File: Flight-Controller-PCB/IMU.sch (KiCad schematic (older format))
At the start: 13 parts, among them Q1 BSS138, Q2 BSS138, U2 ICM-20689

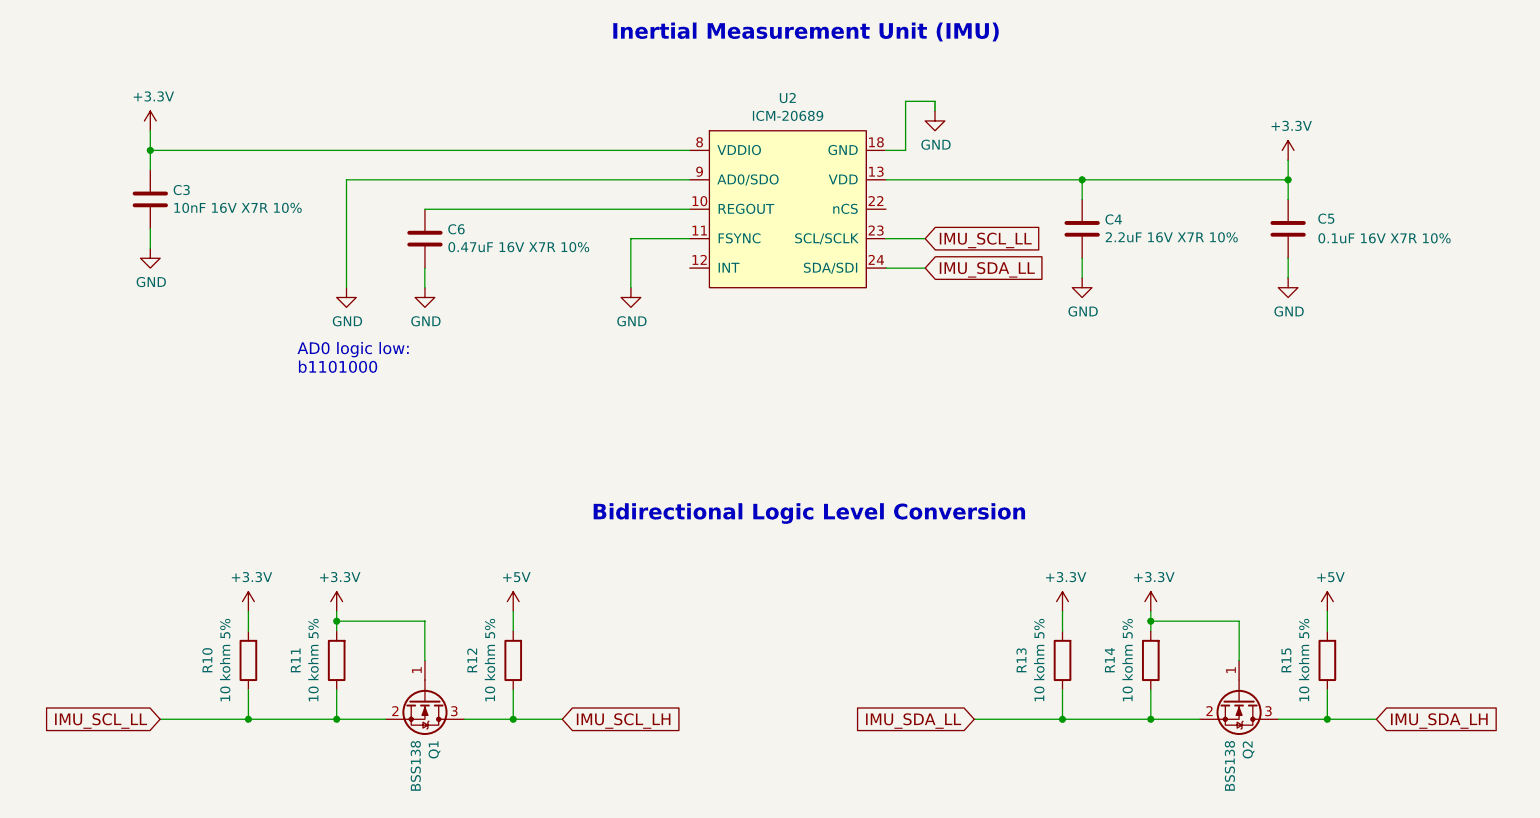
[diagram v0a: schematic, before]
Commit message: Deleted majority of unused components. Started schematic for new MCU
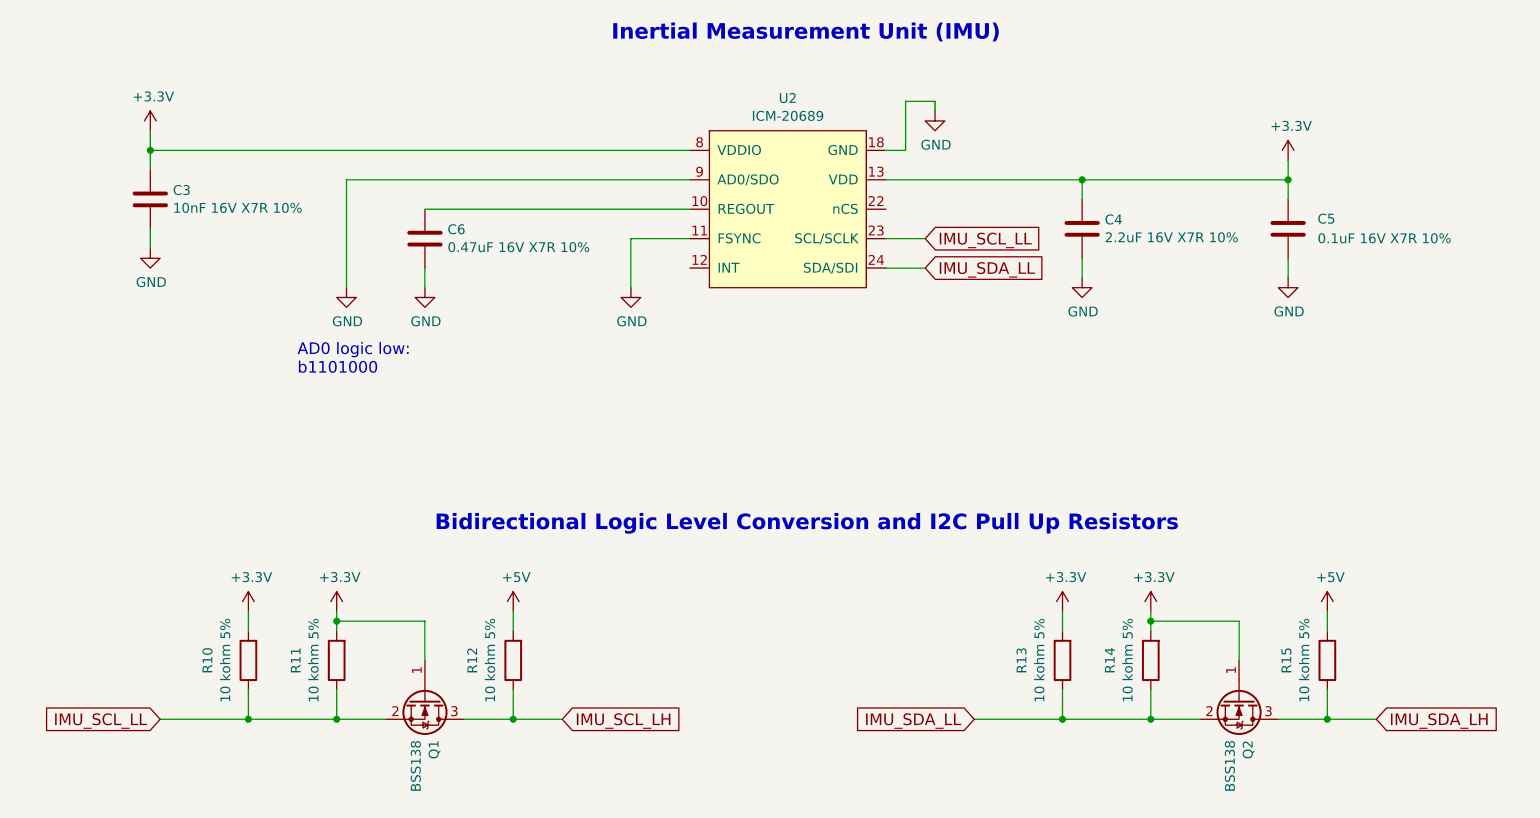
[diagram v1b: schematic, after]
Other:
- note added: "Bidirectional Logic Level Conversion and I2C Pull Up Resistors"
- note removed: "Bidirectional Logic Level Conversion"
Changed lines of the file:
@@
 EESchema Schematic File Version 4
-LIBS:Main-Board-cache
 EELAYER 30 0
 EELAYER END
@@
 Text Notes 4650 1800 0    79   ~ 16
 Inertial Measurement Unit (IMU)
-Text Notes 4550 4250 0    79   ~ 16
-Bidirectional Logic Level Conversion
+Text Notes 3750 4300 0    79   ~ 16
+Bidirectional Logic Level Conversion and I2C Pull Up Resistors
 $EndSCHEMATC

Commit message: Power Management and Selection roughed out
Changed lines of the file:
@@
 AR Path="/5FD99B6C/5FD9D006" Ref="Q1"  Part="1"
 AR Path="/5FD9E07D/5FD9D006" Ref="Q?"  Part="1"
-F 0 "Q1" H 3906 5196 50  0000 L CNN
-F 1 "BSS138" H 3906 5105 50  0000 L CNN
+F 0 "Q1" V 3951 5150 50  0000 C CNN
+F 1 "BSS138" V 4042 5150 50  0000 C CNN
 F 2 "Package_TO_SOT_SMD:SOT-23" H 3900 5075 50  0001 L CIN
 F 3 "" H 3700 5150 50  0001 L CNN
@@
 AR Path="/5FD99B6C/60033880" Ref="Q2"  Part="1"
 AR Path="/5FD9E07D/60033880" Ref="Q?"  Part="1"
-F 0 "Q2" H 8056 5196 50  0000 L CNN
-F 1 "BSS138" H 8056 5105 50  0000 L CNN
+F 0 "Q2" V 8101 5150 50  0000 C CNN
+F 1 "BSS138" V 8192 5150 50  0000 C CNN
 F 2 "Package_TO_SOT_SMD:SOT-23" H 8050 5075 50  0001 L CIN
 F 3 "" H 7850 5150 50  0001 L CNN

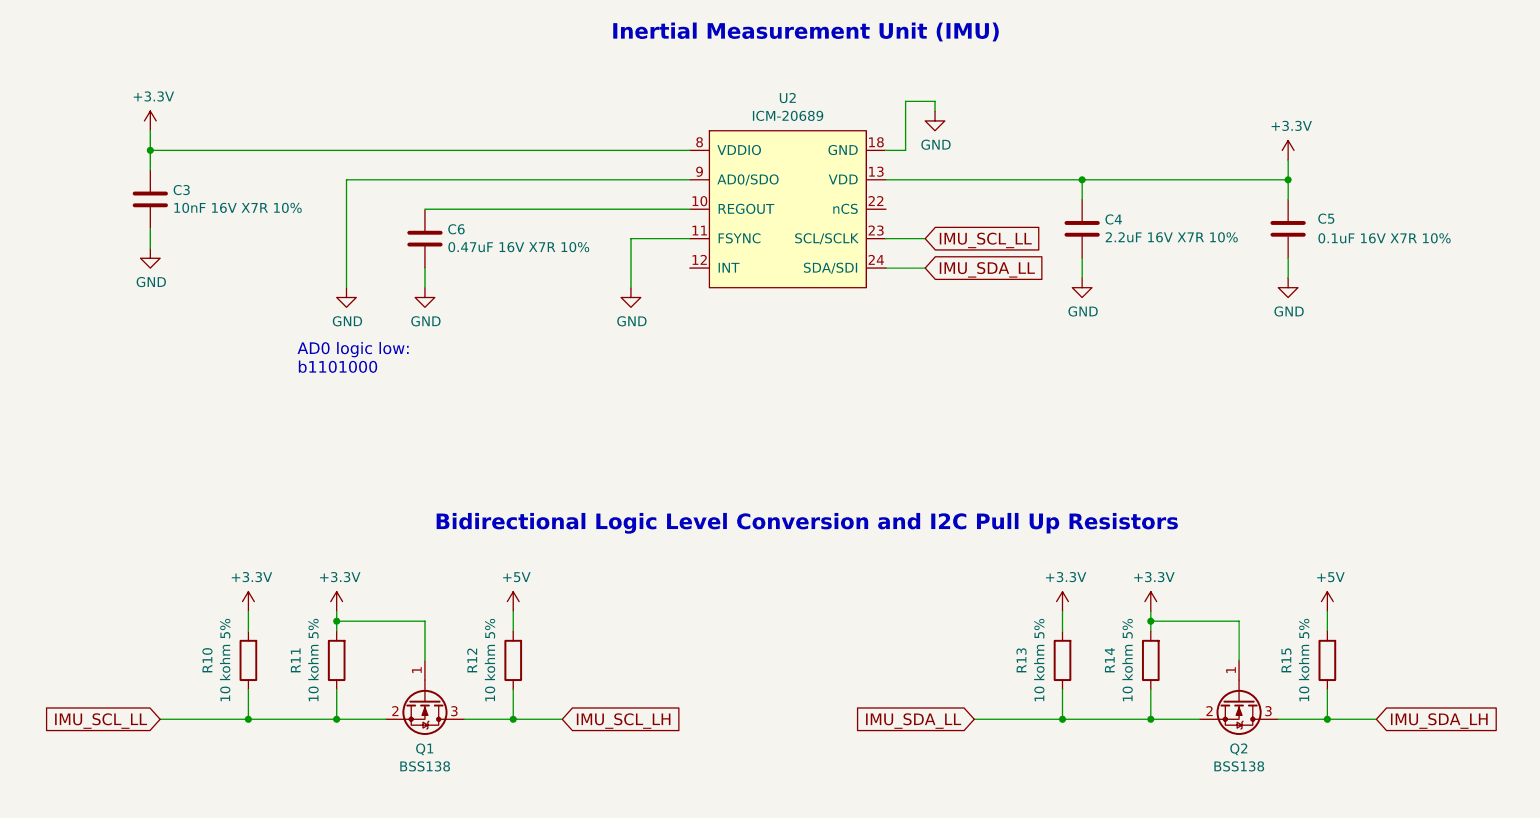
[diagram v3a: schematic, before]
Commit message: Updated pin mappings
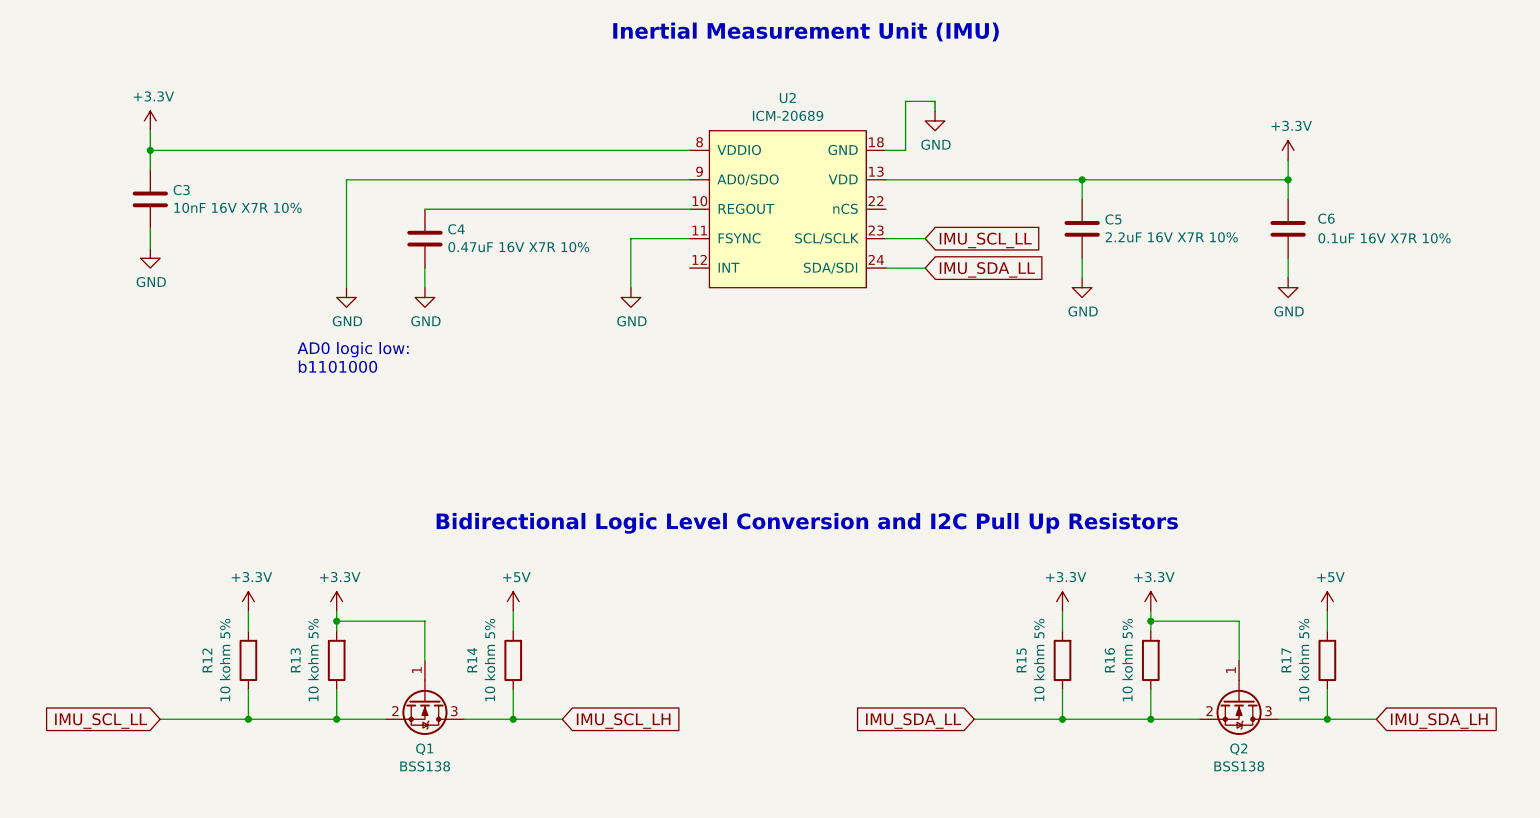
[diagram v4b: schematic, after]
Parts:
- renumbered C6 to C4, C4 to C5, C5 to C6, R10 to R12, R11 to R13, R12 to R14, R13 to R15, R14 to R16, R15 to R17
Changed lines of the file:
@@
 IMU_SCL_LL
 $Comp
-L power:+3.3V #PWR031
+L power:+3.3V #PWR030
 U 1 1 5FD9D00C
 P 2800 4700
-AR Path="/5FD99B6C/5FD9D00C" Ref="#PWR031"  Part="1"
+AR Path="/5FD99B6C/5FD9D00C" Ref="#PWR030"  Part="1"
 AR Path="/5FD9E07D/5FD9D00C" Ref="#PWR?"  Part="1"
-F 0 "#PWR031" H 2800 4550 50  0001 C CNN
+F 0 "#PWR030" H 2800 4550 50  0001 C CNN
 F 1 "+3.3V" H 2815 4873 50  0000 C CNN
 F 2 "" H 2800 4700 50  0001 C CNN
@@
 	5050 2800 4750 2800
 $Comp
-L power:GND #PWR030
+L power:GND #PWR035
 U 1 1 5FD9CFF8
 P 4750 3050
-AR Path="/5FD99B6C/5FD9CFF8" Ref="#PWR030"  Part="1"
+AR Path="/5FD99B6C/5FD9CFF8" Ref="#PWR035"  Part="1"
 AR Path="/5FD9E07D/5FD9CFF8" Ref="#PWR?"  Part="1"
-F 0 "#PWR030" H 4750 2800 50  0001 C CNN
+F 0 "#PWR035" H 4750 2800 50  0001 C CNN
 F 1 "GND" H 4755 2877 50  0000 C CNN
 F 2 "" H 4750 3050 50  0001 C CNN
@@
 	3300 2500 3300 3050
 $Comp
-L power:GND #PWR028
+L power:GND #PWR032
 U 1 1 5FD9CFEF
 P 3300 3050
-AR Path="/5FD99B6C/5FD9CFEF" Ref="#PWR028"  Part="1"
+AR Path="/5FD99B6C/5FD9CFEF" Ref="#PWR032"  Part="1"
 AR Path="/5FD9E07D/5FD9CFEF" Ref="#PWR?"  Part="1"
-F 0 "#PWR028" H 3300 2800 50  0001 C CNN
+F 0 "#PWR032" H 3300 2800 50  0001 C CNN
 F 1 "GND" H 3305 2877 50  0000 C CNN
 F 2 "" H 3300 3050 50  0001 C CNN
@@
 	3700 3050 3700 2950
 $Comp
-L power:GND #PWR029
+L power:GND #PWR033
 U 1 1 5FD9CFE8
 P 3700 3050
-AR Path="/5FD99B6C/5FD9CFE8" Ref="#PWR029"  Part="1"
+AR Path="/5FD99B6C/5FD9CFE8" Ref="#PWR033"  Part="1"
 AR Path="/5FD9E07D/5FD9CFE8" Ref="#PWR?"  Part="1"
-F 0 "#PWR029" H 3700 2800 50  0001 C CNN
+F 0 "#PWR033" H 3700 2800 50  0001 C CNN
 F 1 "GND" H 3705 2877 50  0000 C CNN
 F 2 "" H 3700 3050 50  0001 C CNN
@@
 	6050 2500 7050 2500
 $Comp
-L power:GND #PWR027
+L power:GND #PWR041
 U 1 1 5FD9CFD9
 P 8100 3000
-AR Path="/5FD99B6C/5FD9CFD9" Ref="#PWR027"  Part="1"
+AR Path="/5FD99B6C/5FD9CFD9" Ref="#PWR041"  Part="1"
 AR Path="/5FD9E07D/5FD9CFD9" Ref="#PWR?"  Part="1"
-F 0 "#PWR027" H 8100 2750 50  0001 C CNN
+F 0 "#PWR041" H 8100 2750 50  0001 C CNN
 F 1 "GND" H 8105 2827 50  0000 C CNN
 F 2 "" H 8100 3000 50  0001 C CNN
@@
 $EndComp
 $Comp
-L power:GND #PWR026
+L power:GND #PWR038
 U 1 1 5FD9CFD3
 P 7050 3000
-AR Path="/5FD99B6C/5FD9CFD3" Ref="#PWR026"  Part="1"
+AR Path="/5FD99B6C/5FD9CFD3" Ref="#PWR038"  Part="1"
 AR Path="/5FD9E07D/5FD9CFD3" Ref="#PWR?"  Part="1"
-F 0 "#PWR026" H 7050 2750 50  0001 C CNN
+F 0 "#PWR038" H 7050 2750 50  0001 C CNN
 F 1 "GND" H 7055 2827 50  0000 C CNN
 F 2 "" H 7050 3000 50  0001 C CNN
@@
 	6050 2350 6150 2350
 $Comp
-L power:+3.3V #PWR024
+L power:+3.3V #PWR040
 U 1 1 5FD9CFC9
 P 8100 2400
-AR Path="/5FD99B6C/5FD9CFC9" Ref="#PWR024"  Part="1"
+AR Path="/5FD99B6C/5FD9CFC9" Ref="#PWR040"  Part="1"
 AR Path="/5FD9E07D/5FD9CFC9" Ref="#PWR?"  Part="1"
-F 0 "#PWR024" H 8100 2250 50  0001 C CNN
+F 0 "#PWR040" H 8100 2250 50  0001 C CNN
 F 1 "+3.3V" H 8115 2573 50  0000 C CNN
 F 2 "" H 8100 2400 50  0001 C CNN
@@
 	2300 2250 2300 2350
 $Comp
-L power:GND #PWR025
+L power:GND #PWR029
 U 1 1 5FD9CFBF
 P 2300 2850
-AR Path="/5FD99B6C/5FD9CFBF" Ref="#PWR025"  Part="1"
+AR Path="/5FD99B6C/5FD9CFBF" Ref="#PWR029"  Part="1"
 AR Path="/5FD9E07D/5FD9CFBF" Ref="#PWR?"  Part="1"
-F 0 "#PWR025" H 2300 2600 50  0001 C CNN
+F 0 "#PWR029" H 2300 2600 50  0001 C CNN
 F 1 "GND" H 2305 2677 50  0000 C CNN
 F 2 "" H 2300 2850 50  0001 C CNN
@@
 $EndComp
 $Comp
-L power:+3.3V #PWR023
+L power:+3.3V #PWR028
 U 1 1 5FD9CFB9
 P 2300 2250
-AR Path="/5FD99B6C/5FD9CFB9" Ref="#PWR023"  Part="1"
+AR Path="/5FD99B6C/5FD9CFB9" Ref="#PWR028"  Part="1"
 AR Path="/5FD9E07D/5FD9CFB9" Ref="#PWR?"  Part="1"
-F 0 "#PWR023" H 2300 2100 50  0001 C CNN
+F 0 "#PWR028" H 2300 2100 50  0001 C CNN
 F 1 "+3.3V" H 2315 2423 50  0000 C CNN
 F 2 "" H 2300 2250 50  0001 C CNN
@@
 $EndComp
 $Comp
-L Device:R R10
+L Device:R R12
 U 1 1 5FD9CFB3
 P 2800 4950
-AR Path="/5FD99B6C/5FD9CFB3" Ref="R10"  Part="1"
+AR Path="/5FD99B6C/5FD9CFB3" Ref="R12"  Part="1"
 AR Path="/5FD9E07D/5FD9CFB3" Ref="R?"  Part="1"
-F 0 "R10" V 3007 4950 50  0000 C CNN
+F 0 "R12" V 3007 4950 50  0000 C CNN
 F 1 "10 kohm 5%" V 2916 4950 50  0000 C CNN
 F 2 "Resistor_SMD:R_0603_1608Metric_Pad1.05x0.95mm_HandSolder" V 2730 4950 50  0001 C CNN
@@
 $EndComp
 $Comp
-L power:GND #PWR022
+L power:GND #PWR036
 U 1 1 5FD9CFAD
 P 6300 2150
-AR Path="/5FD99B6C/5FD9CFAD" Ref="#PWR022"  Part="1"
+AR Path="/5FD99B6C/5FD9CFAD" Ref="#PWR036"  Part="1"
 AR Path="/5FD9E07D/5FD9CFAD" Ref="#PWR?"  Part="1"
-F 0 "#PWR022" H 6300 1900 50  0001 C CNN
+F 0 "#PWR036" H 6300 1900 50  0001 C CNN
 F 1 "GND" H 6305 1977 50  0000 C CNN
 F 2 "" H 6300 2150 50  0001 C CNN
@@
 $EndComp
 $Comp
-L Device:C C4
+L Device:C C5
 U 1 1 5FD9CFA1
 P 7050 2750
-AR Path="/5FD99B6C/5FD9CFA1" Ref="C4"  Part="1"
+AR Path="/5FD99B6C/5FD9CFA1" Ref="C5"  Part="1"
 AR Path="/5FD9E07D/5FD9CFA1" Ref="C?"  Part="1"
-F 0 "C4" H 7165 2796 50  0000 L CNN
+F 0 "C5" H 7165 2796 50  0000 L CNN
 F 1 "2.2uF 16V X7R 10%" H 7165 2705 50  0000 L CNN
 F 2 "Capacitor_SMD:C_0603_1608Metric_Pad1.05x0.95mm_HandSolder" H 7088 2600 50  0001 C CNN
@@
 $EndComp
 $Comp
-L Device:C C6
+L Device:C C4
 U 1 1 5FD9CF95
 P 3700 2800
-AR Path="/5FD99B6C/5FD9CF95" Ref="C6"  Part="1"
+AR Path="/5FD99B6C/5FD9CF95" Ref="C4"  Part="1"
 AR Path="/5FD9E07D/5FD9CF95" Ref="C?"  Part="1"
-F 0 "C6" H 3815 2846 50  0000 L CNN
+F 0 "C4" H 3815 2846 50  0000 L CNN
 F 1 "0.47uF 16V X7R 10%" H 3815 2755 50  0000 L CNN
 F 2 "Capacitor_SMD:C_0603_1608Metric_Pad1.05x0.95mm_HandSolder" H 3738 2650 50  0001 C CNN
@@
 $EndComp
 $Comp
-L Device:R R11
+L Device:R R13
 U 1 1 5FDA5523
 P 3250 4950
-AR Path="/5FD99B6C/5FDA5523" Ref="R11"  Part="1"
+AR Path="/5FD99B6C/5FDA5523" Ref="R13"  Part="1"
 AR Path="/5FD9E07D/5FDA5523" Ref="R?"  Part="1"
-F 0 "R11" V 3457 4950 50  0000 C CNN
+F 0 "R13" V 3457 4950 50  0000 C CNN
 F 1 "10 kohm 5%" V 3366 4950 50  0000 C CNN
 F 2 "Resistor_SMD:R_0603_1608Metric_Pad1.05x0.95mm_HandSolder" V 3180 4950 50  0001 C CNN
@@
 $EndComp
 $Comp
-L power:+3.3V #PWR032
+L power:+3.3V #PWR031
 U 1 1 5FDA626A
 P 3250 4700
-AR Path="/5FD99B6C/5FDA626A" Ref="#PWR032"  Part="1"
+AR Path="/5FD99B6C/5FDA626A" Ref="#PWR031"  Part="1"
 AR Path="/5FD9E07D/5FDA626A" Ref="#PWR?"  Part="1"
-F 0 "#PWR032" H 3250 4550 50  0001 C CNN
+F 0 "#PWR031" H 3250 4550 50  0001 C CNN
 F 1 "+3.3V" H 3265 4873 50  0000 C CNN
 F 2 "" H 3250 4700 50  0001 C CNN
@@
 $EndComp
 $Comp
-L Device:R R12
+L Device:R R14
 U 1 1 5FDA6839
 P 4150 4950
-AR Path="/5FD99B6C/5FDA6839" Ref="R12"  Part="1"
+AR Path="/5FD99B6C/5FDA6839" Ref="R14"  Part="1"
 AR Path="/5FD9E07D/5FDA6839" Ref="R?"  Part="1"
-F 0 "R12" V 4357 4950 50  0000 C CNN
+F 0 "R14" V 4357 4950 50  0000 C CNN
 F 1 "10 kohm 5%" V 4266 4950 50  0000 C CNN
 F 2 "Resistor_SMD:R_0603_1608Metric_Pad1.05x0.95mm_HandSolder" V 4080 4950 50  0001 C CNN
@@
 $EndComp
 $Comp
-L power:+5V #PWR033
+L power:+5V #PWR034
 U 1 1 5FDA6B36
 P 4150 4700
-F 0 "#PWR033" H 4150 4550 50  0001 C CNN
+F 0 "#PWR034" H 4150 4550 50  0001 C CNN
 F 1 "+5V" H 4165 4873 50  0000 C CNN
 F 2 "" H 4150 4700 50  0001 C CNN
@@
 	2800 4800 2800 4700
 $Comp
-L power:+3.3V #PWR034
+L power:+3.3V #PWR037
 U 1 1 5FDB9369
 P 6950 4700
-AR Path="/5FD99B6C/5FDB9369" Ref="#PWR034"  Part="1"
+AR Path="/5FD99B6C/5FDB9369" Ref="#PWR037"  Part="1"
 AR Path="/5FD9E07D/5FDB9369" Ref="#PWR?"  Part="1"
-F 0 "#PWR034" H 6950 4550 50  0001 C CNN
+F 0 "#PWR037" H 6950 4550 50  0001 C CNN
 F 1 "+3.3V" H 6965 4873 50  0000 C CNN
 F 2 "" H 6950 4700 50  0001 C CNN
@@
 $EndComp
 $Comp
-L Device:R R13
+L Device:R R15
 U 1 1 5FDB9375
 P 6950 4950
-AR Path="/5FD99B6C/5FDB9375" Ref="R13"  Part="1"
+AR Path="/5FD99B6C/5FDB9375" Ref="R15"  Part="1"
 AR Path="/5FD9E07D/5FDB9375" Ref="R?"  Part="1"
-F 0 "R13" V 7157 4950 50  0000 C CNN
+F 0 "R15" V 7157 4950 50  0000 C CNN
 F 1 "10 kohm 5%" V 7066 4950 50  0000 C CNN
 F 2 "Resistor_SMD:R_0603_1608Metric_Pad1.05x0.95mm_HandSolder" V 6880 4950 50  0001 C CNN
@@
 $EndComp
 $Comp
-L Device:R R14
+L Device:R R16
 U 1 1 5FDB937B
 P 7400 4950
-AR Path="/5FD99B6C/5FDB937B" Ref="R14"  Part="1"
+AR Path="/5FD99B6C/5FDB937B" Ref="R16"  Part="1"
 AR Path="/5FD9E07D/5FDB937B" Ref="R?"  Part="1"
-F 0 "R14" V 7607 4950 50  0000 C CNN
+F 0 "R16" V 7607 4950 50  0000 C CNN
 F 1 "10 kohm 5%" V 7516 4950 50  0000 C CNN
 F 2 "Resistor_SMD:R_0603_1608Metric_Pad1.05x0.95mm_HandSolder" V 7330 4950 50  0001 C CNN
@@
 $EndComp
 $Comp
-L power:+3.3V #PWR035
+L power:+3.3V #PWR039
 U 1 1 5FDB9381
 P 7400 4700
-AR Path="/5FD99B6C/5FDB9381" Ref="#PWR035"  Part="1"
+AR Path="/5FD99B6C/5FDB9381" Ref="#PWR039"  Part="1"
 AR Path="/5FD9E07D/5FDB9381" Ref="#PWR?"  Part="1"
-F 0 "#PWR035" H 7400 4550 50  0001 C CNN
+F 0 "#PWR039" H 7400 4550 50  0001 C CNN
 F 1 "+3.3V" H 7415 4873 50  0000 C CNN
 F 2 "" H 7400 4700 50  0001 C CNN
@@
 $EndComp
 $Comp
-L Device:R R15
+L Device:R R17
 U 1 1 5FDB9387
 P 8300 4950
-AR Path="/5FD99B6C/5FDB9387" Ref="R15"  Part="1"
+AR Path="/5FD99B6C/5FDB9387" Ref="R17"  Part="1"
 AR Path="/5FD9E07D/5FDB9387" Ref="R?"  Part="1"
-F 0 "R15" V 8507 4950 50  0000 C CNN
+F 0 "R17" V 8507 4950 50  0000 C CNN
 F 1 "10 kohm 5%" V 8416 4950 50  0000 C CNN
 F 2 "Resistor_SMD:R_0603_1608Metric_Pad1.05x0.95mm_HandSolder" V 8230 4950 50  0001 C CNN
@@
 $EndComp
 $Comp
-L power:+5V #PWR036
+L power:+5V #PWR042
 U 1 1 5FDB938D
 P 8300 4700
-F 0 "#PWR036" H 8300 4550 50  0001 C CNN
+F 0 "#PWR042" H 8300 4550 50  0001 C CNN
 F 1 "+5V" H 8315 4873 50  0000 C CNN
 F 2 "" H 8300 4700 50  0001 C CNN
@@
 IMU_SDA_LH
 $Comp
-L Device:C C5
+L Device:C C6
 U 1 1 6001E3D4
 P 8100 2750
-AR Path="/5FD99B6C/6001E3D4" Ref="C5"  Part="1"
+AR Path="/5FD99B6C/6001E3D4" Ref="C6"  Part="1"
 AR Path="/5FD9E07D/6001E3D4" Ref="C?"  Part="1"
 AR Path="/5FDD4B9C/6001E3D4" Ref="C?"  Part="1"
 AR Path="/6001E3D4" Ref="C?"  Part="1"
-F 0 "C5" H 8250 2700 50  0000 L CNN
+F 0 "C6" H 8250 2700 50  0000 L CNN
 F 1 "0.1uF 16V X7R 10%" H 8250 2800 50  0000 L CNN
 F 2 "Capacitor_SMD:C_0603_1608Metric_Pad1.05x0.95mm_HandSolder" H 8138 2600 50  0001 C CNN
